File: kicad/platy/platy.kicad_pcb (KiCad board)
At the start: 2 copper layers, 125.8 x 52.6 mm, 92 parts, among them J1 Conn_01x04_Socket, J2 Conn_01x02_Socket, J3 Conn_Coaxial, J5 USB_C_Receptacle_USB2.0_16P, J6 Conn_01x05_Pin, J8 Conn_01x14_Socket, J9 Conn_02x04_Odd_Even, Q4 BC847, Q5 Q_PMOS_GSD, SW2 SW_Push(Boot), SW3 SW_Push(EN), U10 ESP32-S3-WROOM-1, U4 CC1101, U5 PN5321A3HN_C1xx, U6 TSOP382xx, U7 AMS1117-3.3, Y2 27.12Mhz, Y3 26MHz

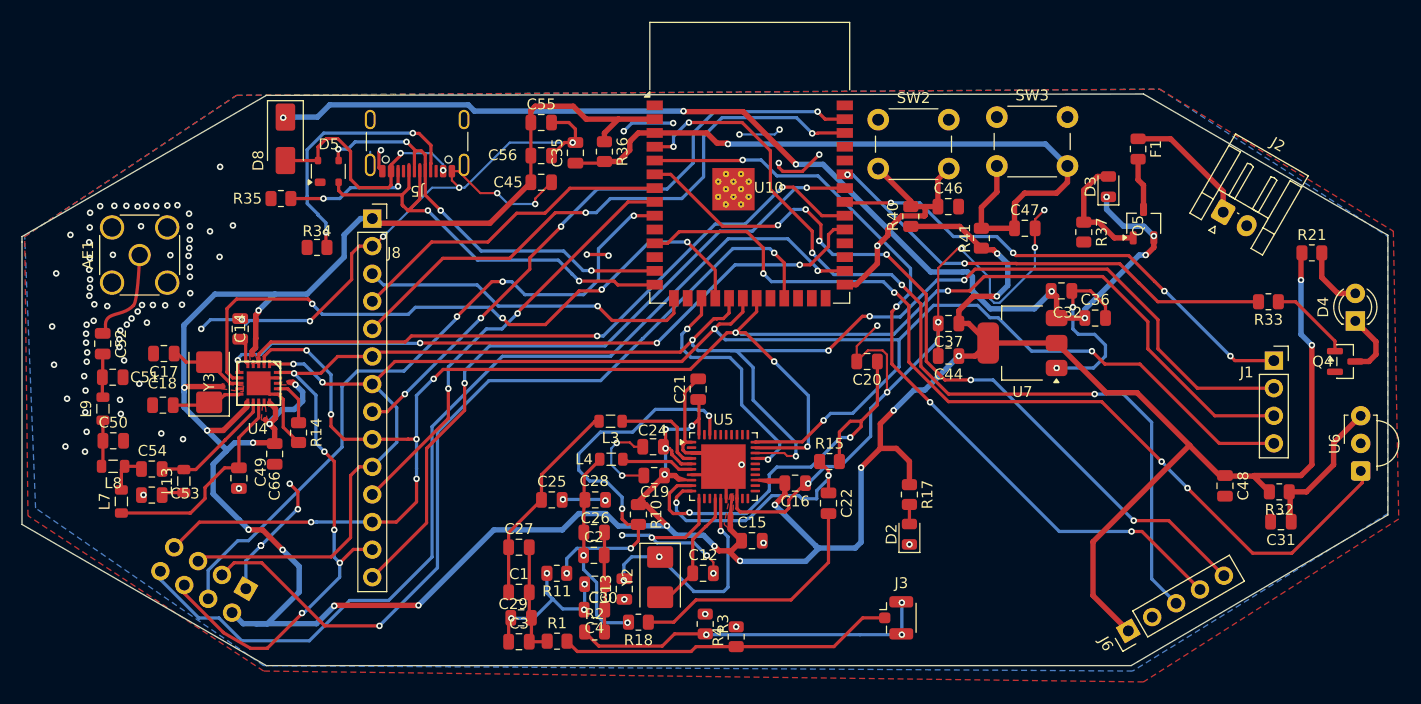
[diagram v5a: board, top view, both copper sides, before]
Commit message: changes in the d+ and d- width and the make the traces curve
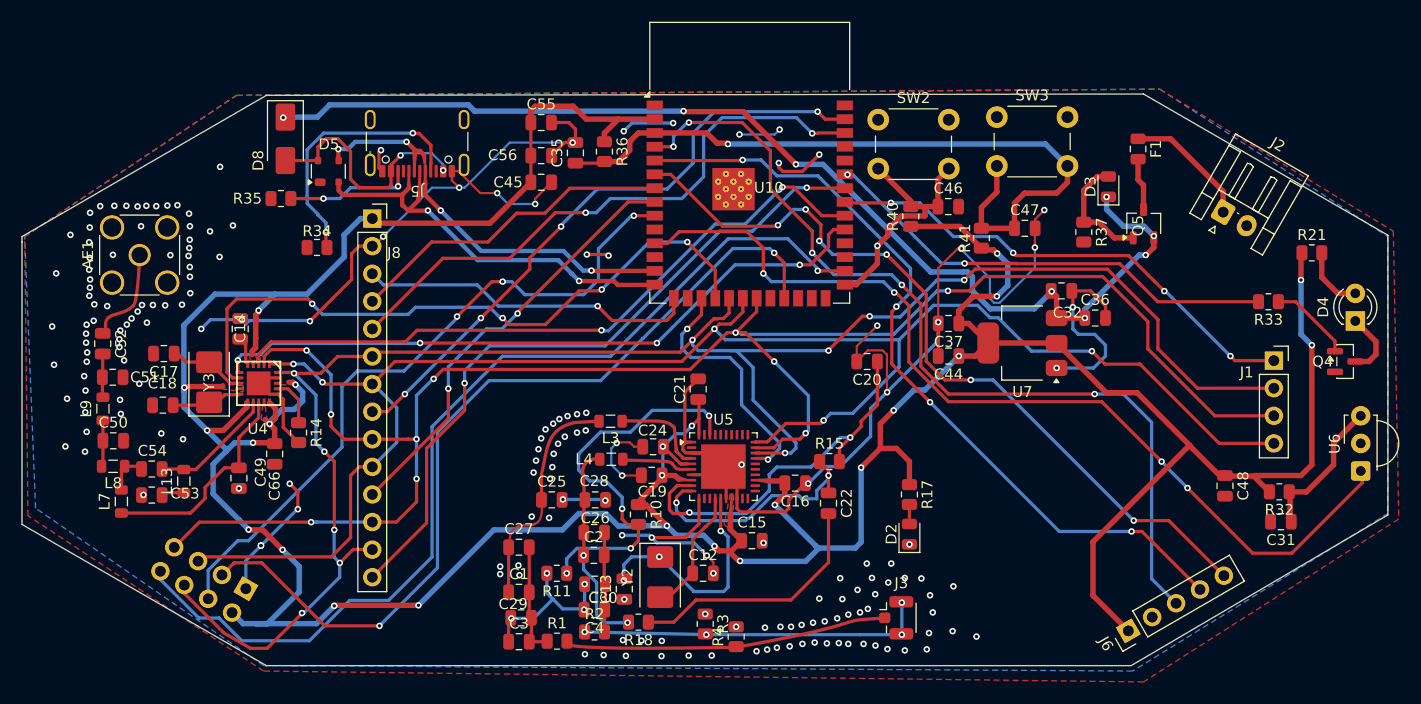
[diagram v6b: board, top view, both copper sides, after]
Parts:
- moved C19 0.23 mm to (152.7, 100.0)
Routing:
- net Net-(J3-In): track 30.9 -> 0.00 mm
- net Net-(C1-Pad1): track 19.4 -> 6.47 mm
- net Net-(J3-Ext): track 33.1 -> 21.0 mm, vias 3 -> 4
- net Net-(U5-TX1): track 9.14 -> 1.92 mm
- net Net-(U5-TX2): track 6.43 -> 0.00 mm
- net /USB_D+: track 41.8 -> 36.6 mm
- net Net-(C2-Pad1): track 18.6 -> 14.4 mm
- net /USB_D-: track 38.8 -> 34.8 mm
- net Net-(U5-VMID): track 37.7 -> 35.2 mm
- net /MOSI: track 168.4 -> 167.5 mm
- net /MISO: track 167.6 -> 166.8 mm
- net /3v3: track 360.6 -> 359.9 mm, vias 25 -> 24
- net GND: vias 117 -> 190

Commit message: change the trace width of the communication traces
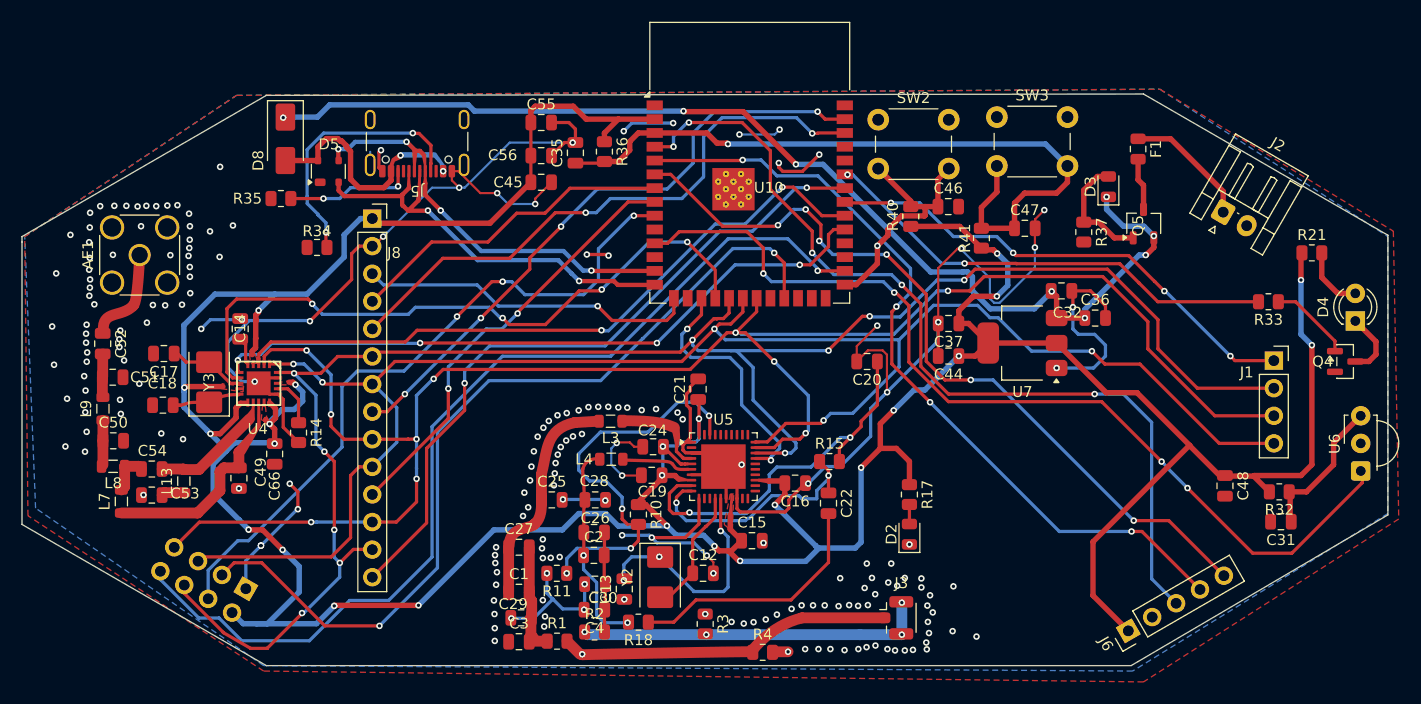
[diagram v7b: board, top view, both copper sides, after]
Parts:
- moved R4 2.83 mm to (162.9, 116.3), turned to 0 degrees
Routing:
- net Net-(J3-Ext): track 21.0 -> 32.3 mm
- net Net-(J3-In): track 0.00 -> 9.60 mm, vias 0 -> 1
- net GND: track 251.0 -> 258.4 mm, vias 190 -> 203
- net Net-(U4-RF_N): track 19.9 -> 15.1 mm
- net Net-(U4-XOSC_Q2): track 5.79 -> 1.12 mm
- net Net-(D8-A): track 22.8 -> 18.9 mm
- net Net-(U4-RF_P): track 11.9 -> 10.4 mm
- net /3v3: track 359.9 -> 361.0 mm
- net Net-(U5-TX1): track 1.92 -> 2.84 mm
- net /RSTPD_N: track 36.0 -> 36.6 mm
- net Net-(C1-Pad2): track 10.5 -> 11.1 mm

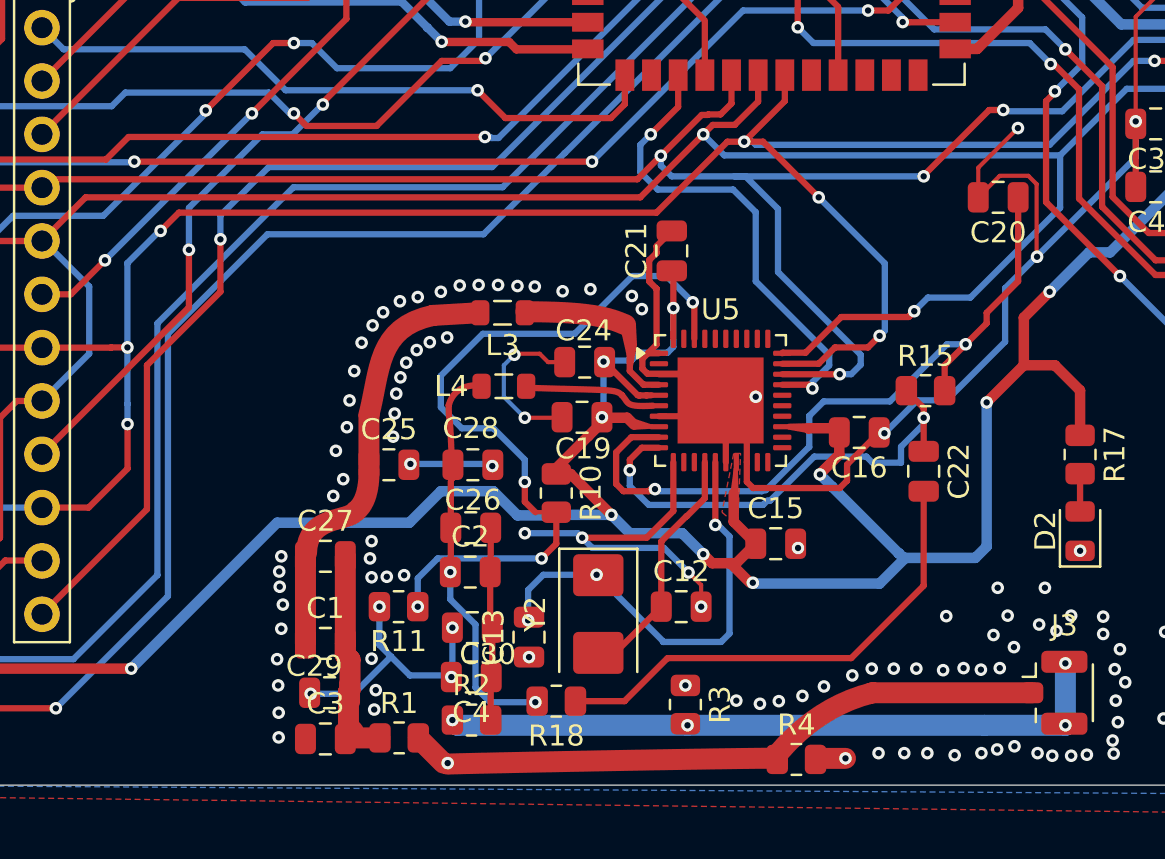
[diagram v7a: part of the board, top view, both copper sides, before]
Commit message: changes made in the placement of the RX
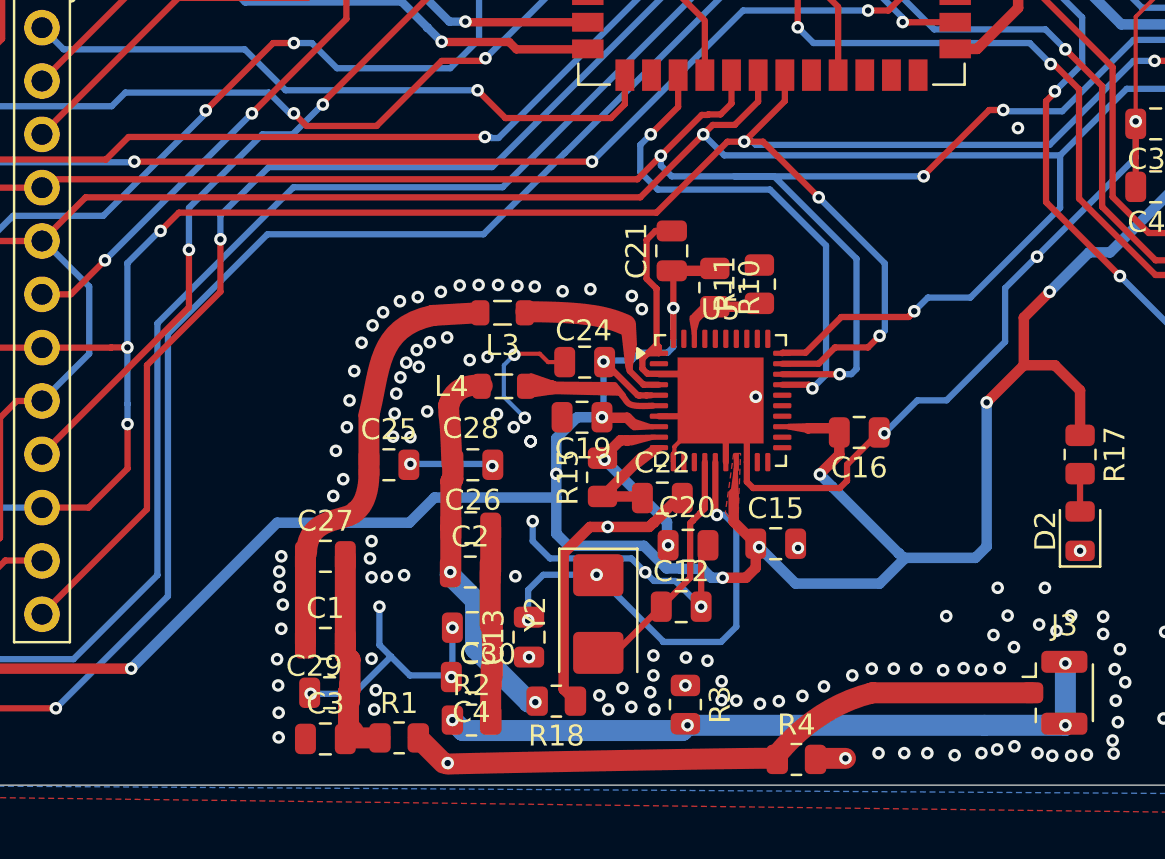
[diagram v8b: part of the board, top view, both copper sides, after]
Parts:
- moved R11 23.1 mm to (161.2, 93.6), turned to 90 degrees
- moved C20 22.2 mm to (157.8, 106.1), turned to 0 degrees
- moved R15 15.9 mm to (153.7, 102.8), turned to 90 degrees
- moved C22 12.5 mm to (156.6, 103.8), turned to 0 degrees
- moved R10 12.4 mm to (159.1, 93.8)
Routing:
- net /RSTPD_N: track 36.6 -> 3.30 mm, vias 4 -> 0
- net Net-(U5-VMID): track 35.2 -> 6.89 mm
- net Net-(U5-RX): track 23.1 -> 4.58 mm, vias 2 -> 0
- net GND: track 258.4 -> 246.0 mm, vias 203 -> 224
- net Net-(C22-Pad2): track 23.4 -> 14.0 mm, vias 0 -> 1
- net /3v3: track 361.0 -> 362.5 mm
- net Net-(C2-Pad1): track 14.4 -> 13.3 mm
- net /SSEL: track 23.3 -> 24.2 mm
- net /MOSI: track 167.5 -> 168.1 mm
